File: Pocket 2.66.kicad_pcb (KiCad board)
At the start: 4 copper layers, 45 x 29.2 mm, 85 parts, among them P1 USB-TYPE-C-018, P3 FPC-05F-24PH20, P4 HX-1.25-2AWB, Q1 HL2300, Q2 HL2305, SW1 TS-24CA-S16, SW2 TS-24CA-S16, SW3 TS-24CA-S16, U1 ESP32-C3FH4, U2 LCK-TF-027H30008-WLG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

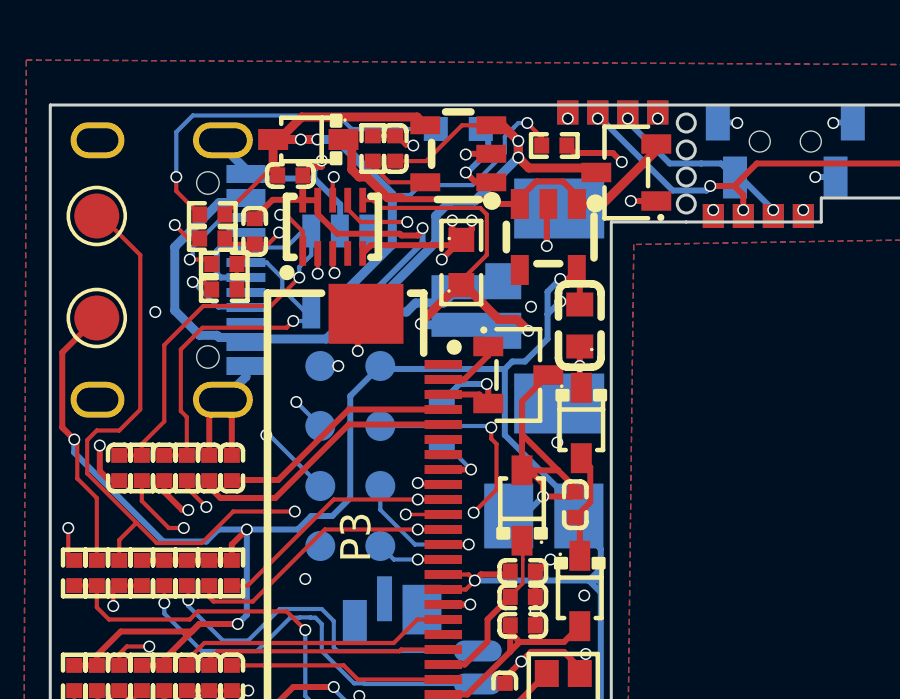
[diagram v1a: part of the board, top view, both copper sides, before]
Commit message: Move 2R2 basic part to top side
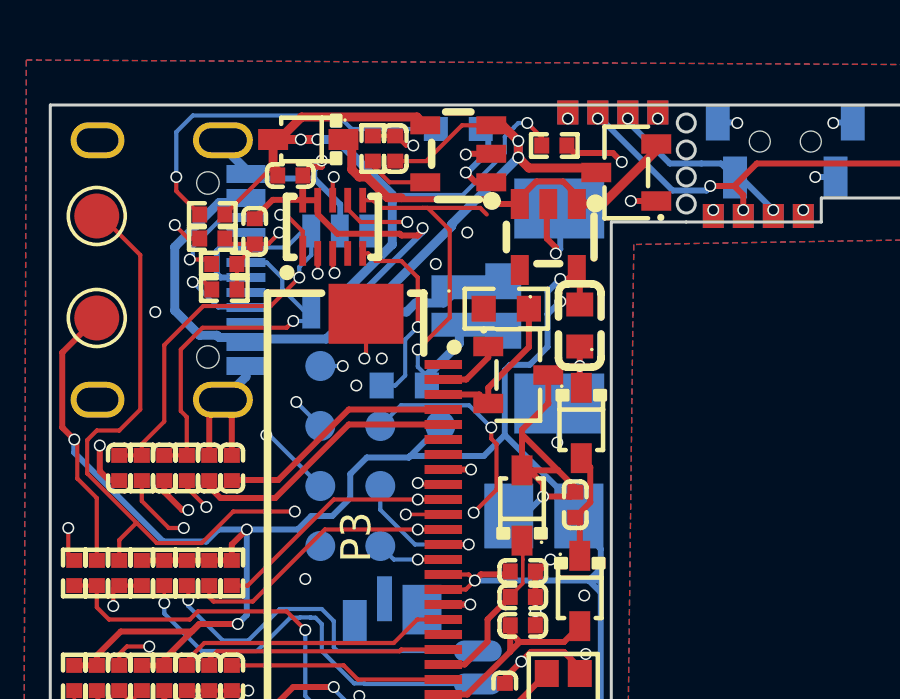
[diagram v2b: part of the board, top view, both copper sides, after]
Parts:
- R1: moved to F.Cu
- SH2: moved to B.Cu
- moved SH2 4.52 mm to (111.8, 80.2), turned to 0 degrees
- moved R1 4.42 mm to (115.2, 77.6), turned to 180 degrees
- moved TP9 2.83 mm to (113.0, 81.5)
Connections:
- TP1 pad 1: /DIS_DC -> /FLEX
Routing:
- net /RESE: track 4.04 -> 5.34 mm, vias 1 -> 0
- net /VBAT-: track 15.5 -> 14.7 mm, vias 2 -> 1
- net /BUT: track 53.8 -> 54.5 mm
- net 3V3: track 123.4 -> 122.8 mm
- net /BOOT: track 54.6 -> 55.2 mm
- net GND: track 85.3 -> 85.1 mm, vias 91 -> 92

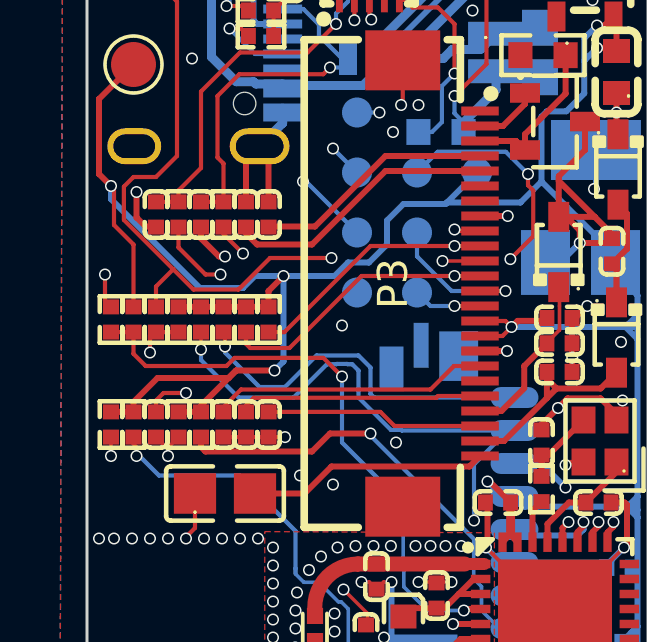
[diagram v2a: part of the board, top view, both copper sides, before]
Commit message: remove vias from serial no. area
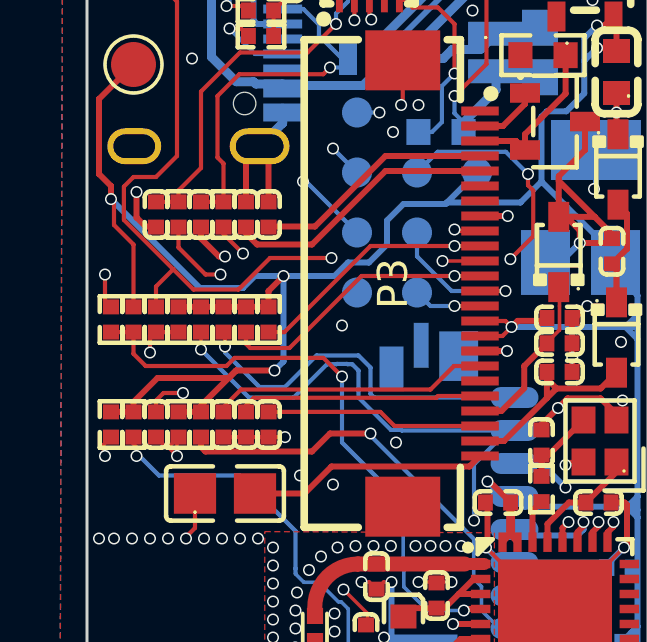
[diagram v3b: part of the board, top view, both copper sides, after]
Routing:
- net /EN: track 43.6 -> 44.1 mm

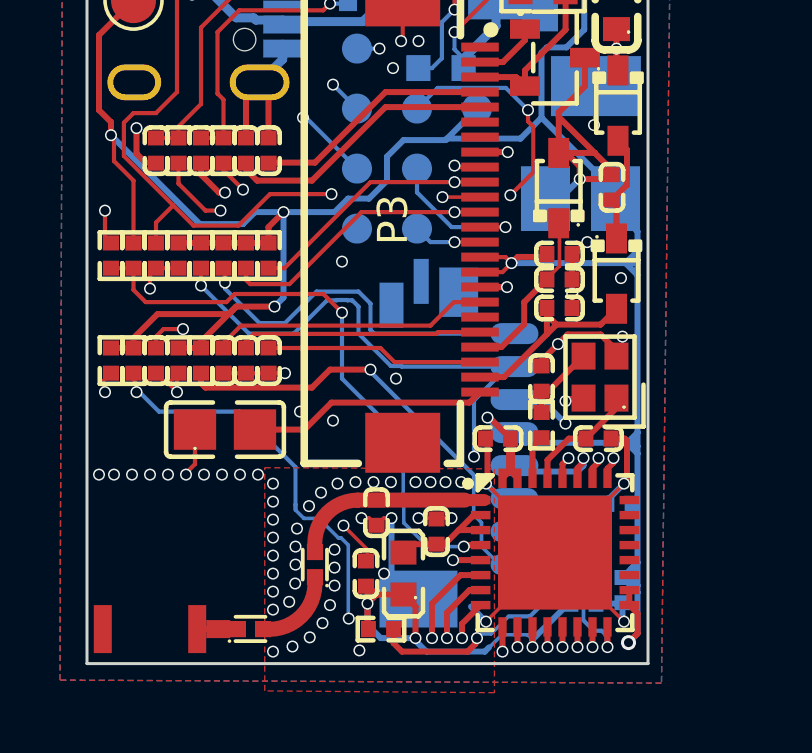
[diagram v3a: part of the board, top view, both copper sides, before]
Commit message: Add extra test pads
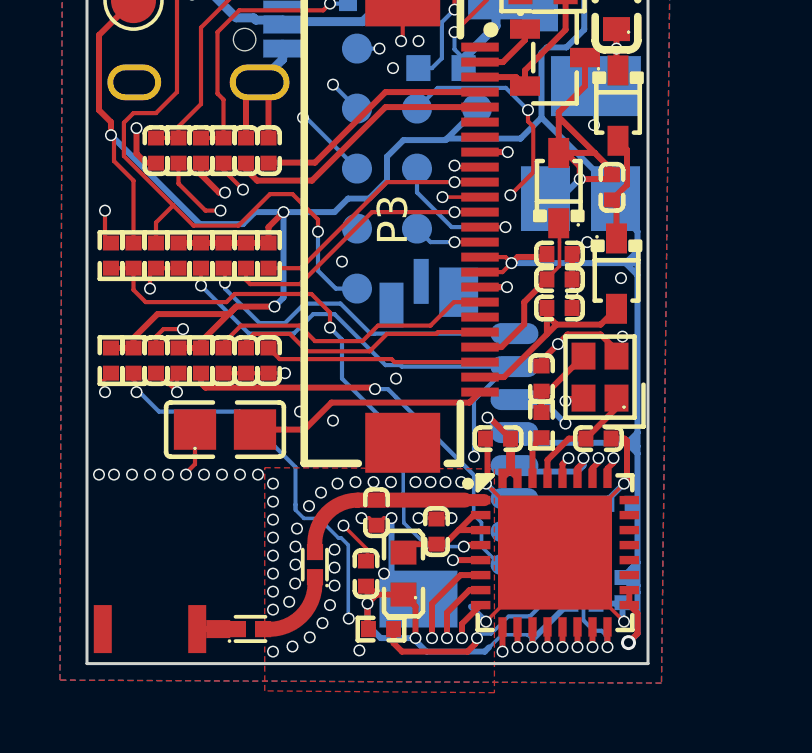
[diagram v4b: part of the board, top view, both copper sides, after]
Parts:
- added TP11: TestPoint, TestPoint:TestPoint_Pad_D1.0mm, B.Cu at (109.0, 87.5)
- added TP12: TestPoint, TestPoint:TestPoint_Pad_D1.0mm, B.Cu at (116.3, 96.9)
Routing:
- net /FLEX: track 38.9 -> 41.0 mm
- net /SD_CS: track 22.4 -> 21.5 mm
- net /DAT2: track 12.4 -> 11.5 mm
- net /DAT1: track 15.1 -> 14.5 mm

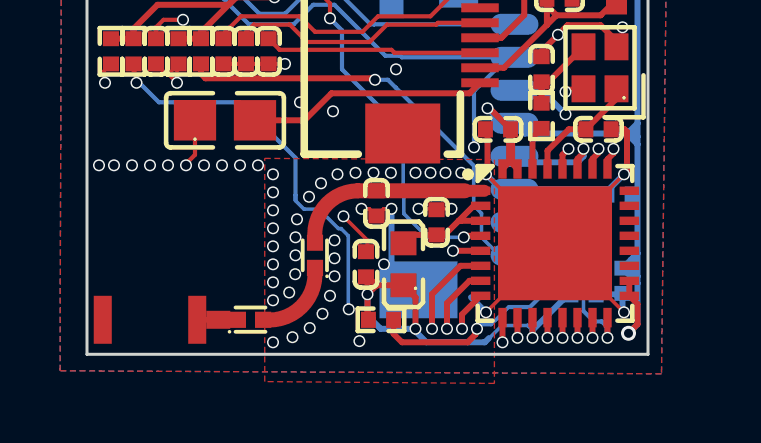
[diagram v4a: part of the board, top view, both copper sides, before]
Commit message: Add second RF shunt (DNP) for extra matching flexibility
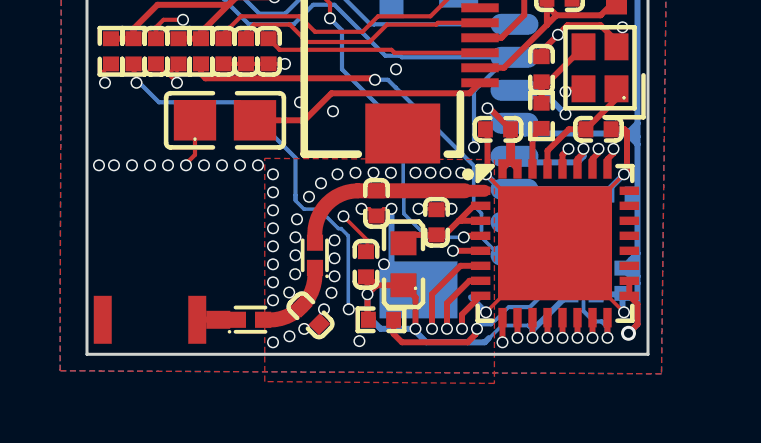
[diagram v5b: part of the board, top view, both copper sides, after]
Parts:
- added C23: 0.7pF 0402, LCSC:C0402, F.Cu at (107.5, 98.7)

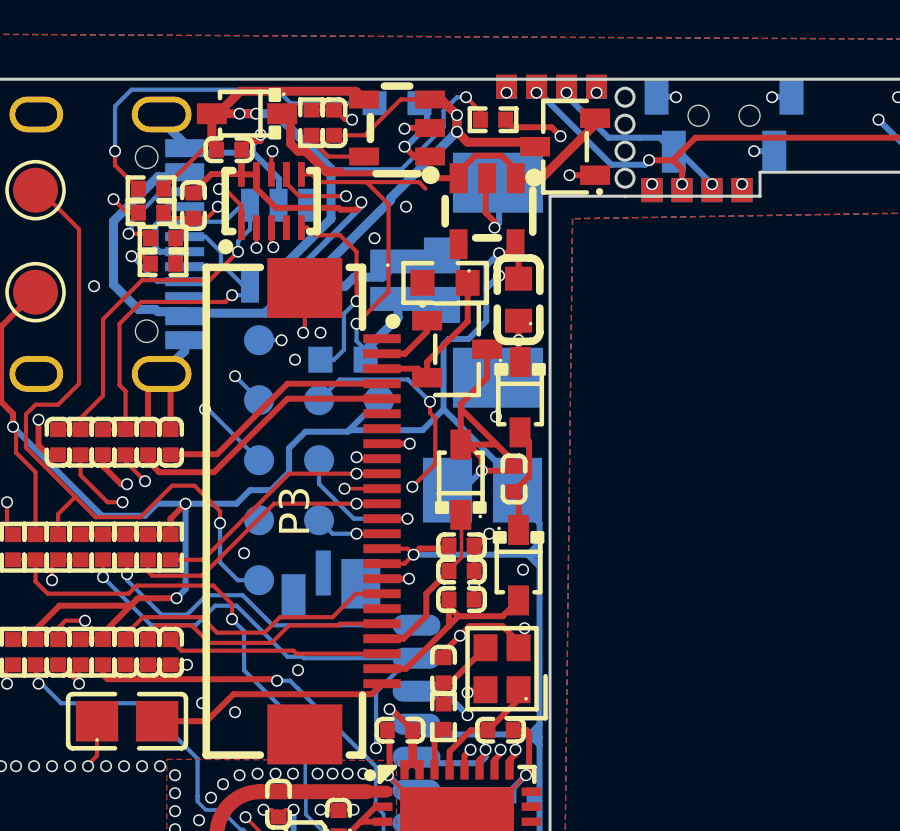
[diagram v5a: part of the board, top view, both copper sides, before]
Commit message: Remove floating traces
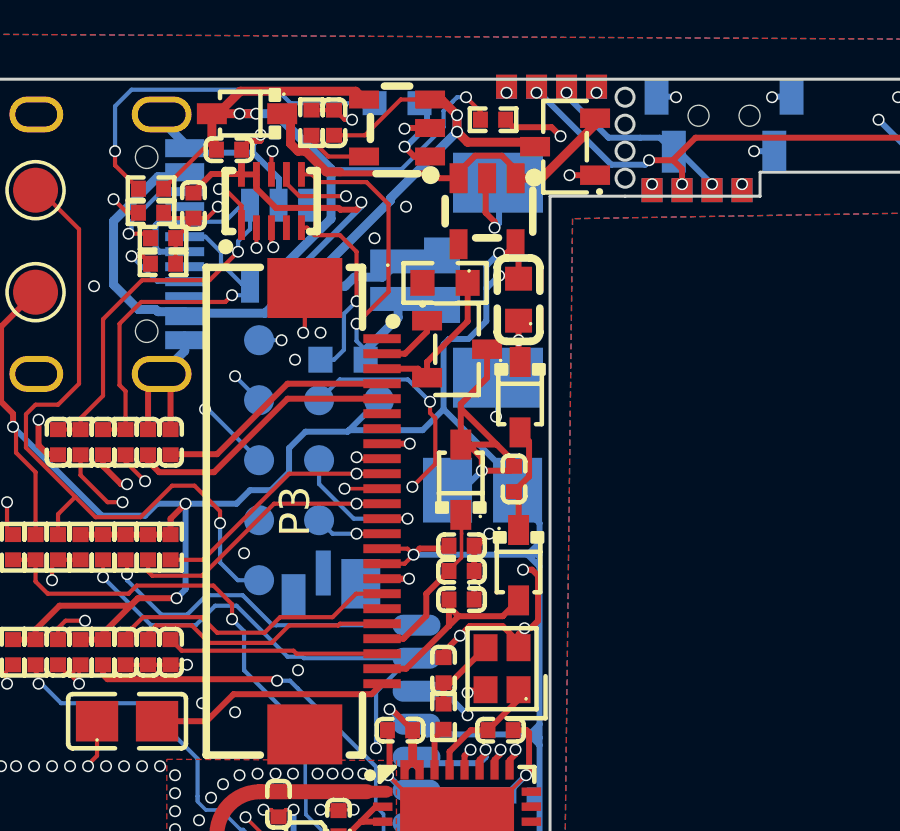
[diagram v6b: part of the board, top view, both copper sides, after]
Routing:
- net GND: track 85.0 -> 88.3 mm
- net /VBAT-: track 14.7 -> 12.4 mm
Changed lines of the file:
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@@
 	)
 	(segment
+		(start 118.05 89.1)
+		(end 118.3 88.85)
+		(width 0.2)
+		(layer "F.Cu")
+		(net "GND")
+	)
+	(segment
 		(start 113.1 87.450064)
 		(end 113.999936 87.450064)
@@
 	)
 	(segment
+		(start 118.3 88.85)
+		(end 118.3 87.35)
+		(width 0.2)
+		(layer "F.Cu")
+		(net "GND")
+	)
+	(segment
 		(start 106.05 82.479883)
 		(end 106.05 80.920873)
@@
 	)
 	(segment
+		(start 117.649911 89.749975)
+		(end 117.649911 89.300089)
+		(width 0.2)
+		(layer "F.Cu")
+		(net "GND")
+	)
+	(segment
 		(start 115.7 89.35)
 		(end 115.15 89.9)
@@
 	)
 	(segment
+		(start 117.649911 89.300089)
+		(end 117.85 89.1)
+		(width 0.2)
+		(layer "F.Cu")
+		(net "GND")
+	)
+	(segment
 		(start 115.6 96.3)
 		(end 117.75 98.45)
@@
 	)
 	(segment
+		(start 117.85 89.1)
+		(end 118.05 89.1)
+		(width 0.2)
+		(layer "F.Cu")
+		(net "GND")
+	)
+	(segment
 		(start 112.25 76.55)
 		(end 112.25 78.2)
@@
 	)
 	(segment
+		(start 118.1 87.15)
+		(end 117.8 87.15)
+		(width 0.2)
+		(layer "F.Cu")
+		(net "GND")
+	)
+	(segment
 		(start 116.275 86.35)
 		(end 116.675 85.95)
@@
 	)
 	(segment
+		(start 118.3 87.35)
+		(end 118.1 87.15)
+		(width 0.2)
+		(layer "F.Cu")
+		(net "GND")
+	)
+	(segment
 		(start 117.65 78.650025)
 		(end 117.65 80.177534)
@@
 	)
 	(segment
-		(start 114.55 74.45)
-		(end 114.33 74.23)
-		(width 0.14)
-		(layer "F.Cu")
-		(net "/VBAT-")
-	)
-	(segment
 		(start 112.58 74.23)
 		(end 112.4 74.23)
@@
 		(width 0.14)
 		(layer "F.Cu")
-		(net "/VBAT-")
-	)
-	(segment
-		(start 114.33 74.23)
-		(end 112.4 74.23)
-		(width 0.14)
-		(layer "F.Cu")

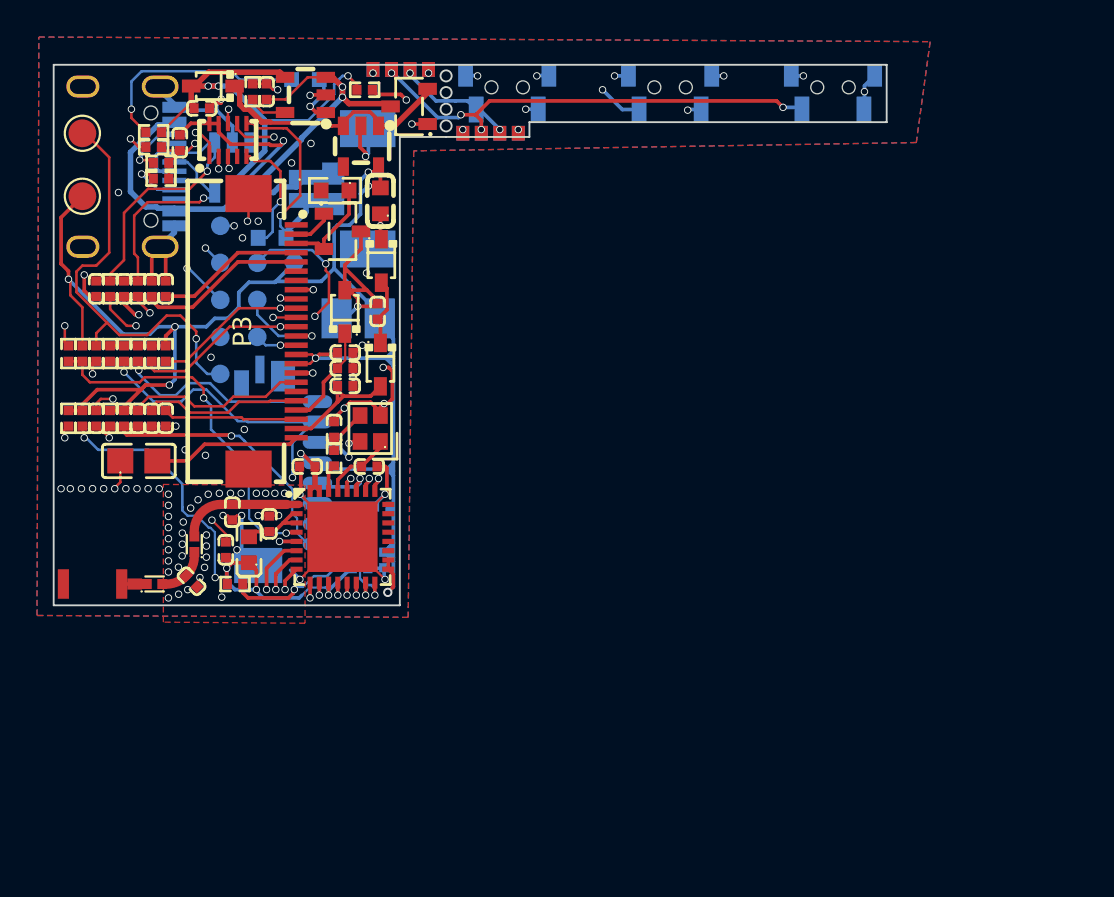
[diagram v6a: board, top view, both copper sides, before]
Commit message: Schematics for ESP32-C3 mini module
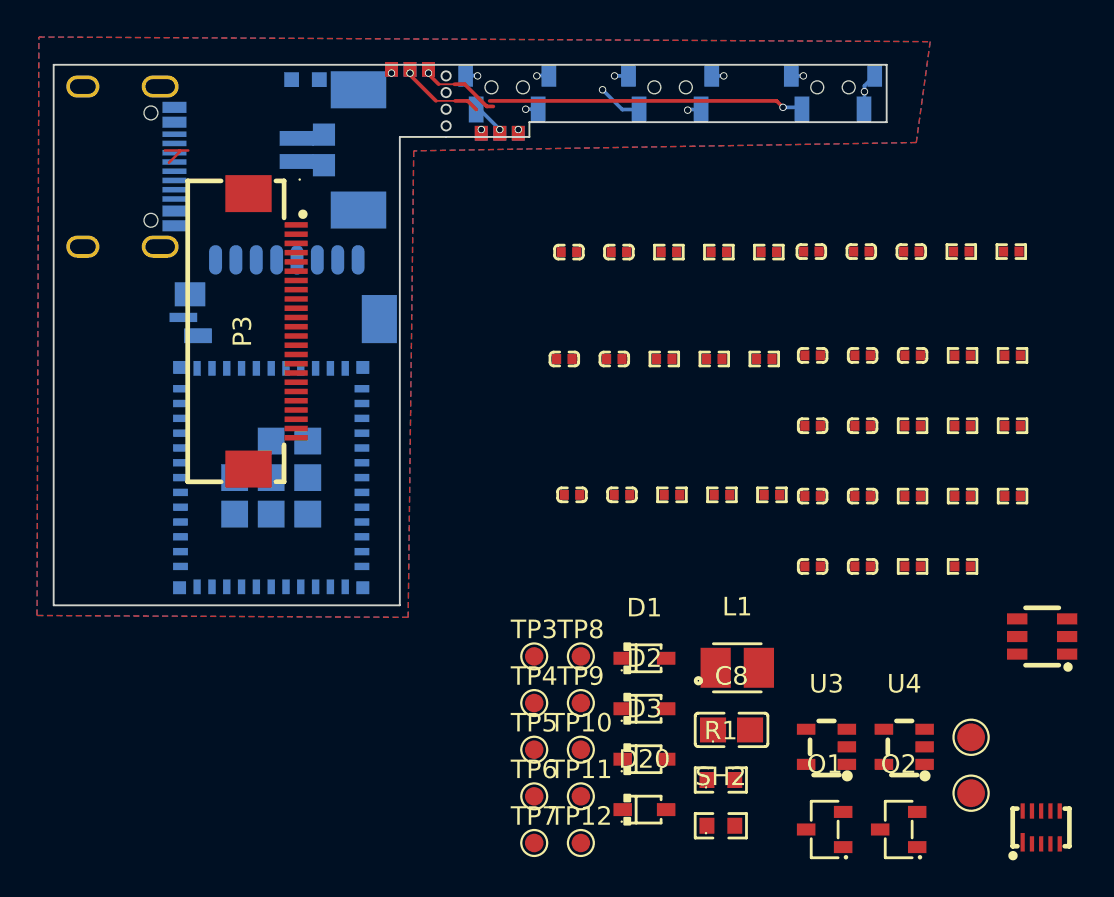
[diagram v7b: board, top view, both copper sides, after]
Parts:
- removed ANT2: 2.45 Ghz 1206, LCSC:SMD_ANT_1206
- removed C10: 0.7pF 0402, LCSC:C0402
- removed C14, C15, C18: 1uF, LCSC:C0402
- removed C16, C17: 15pF, LCSC:C0402
- removed C19, C24: 4.7uF 10V, LCSC:C0402
- removed FB1: BLM18PG121SN1D_C14709, LCSC:C14709_L0603
- removed L2: 8.2nH 0402, LCSC:L0402
- removed L3: 1.6nH 0402, LCSC:L0402
- removed R15, R16, R17: 10KΩ, LCSC:R0402
- removed X1: 40MHz 9pF 2016, LCSC:C49304717_CRYSTAL-SMD_4P-L2_0-W1_6-BL
- added R24: 10KΩ, LCSC:R0402, F.Cu at (151.8, 94.1)
- added R4: 10KΩ, LCSC:R0402, F.Cu at (133.0, 86.7)
- C11, C12: value 1uF -> 4.7uF 10V
- C13, L1, SH2, TP10, TP11, TP12, TP3, TP4, TP5, TP6, TP7, TP8, TP9, U6: moved to F.Cu
- C21: value 22uF -> 4.7uF 10V; footprint LCSC:C59461_C0603 -> LCSC:C0402
- C23: value 0.7pF 0402 -> 4.7uF 10V
- R18: value 22Ω -> 10KΩ
- U1: value ESP32-C3FH4 -> ESP32-C3-MINI-1-N4; footprint LCSC:C2858491_QFN-32_L5_0-W5_0-P0_50-TL-EP3_7 -> LCSC:C2838502_WIFIM-SMD_ESP32-C3-MINI-1; moved to B.Cu
- moved TP1 58.0 mm to (149.6, 107.1)
- moved TP2 57.8 mm to (149.6, 110.2)
- moved U5 57.5 mm to (153.3, 112.0)
- moved U6 50.6 mm to (153.4, 101.7), turned to 0 degrees
- moved R8 48.3 mm to (149.0, 80.9), turned to 0 degrees
- moved Q2 47.2 mm to (145.7, 112.1)
- moved R19 46.7 mm to (151.7, 80.9)
- moved R5 45.8 mm to (146.4, 94.1), turned to 0 degrees
- moved D20 45.5 mm to (131.9, 111.0), turned to 0 degrees
- moved R13 45.5 mm to (149.1, 94.1), turned to 0 degrees
- moved R11 45.5 mm to (149.1, 90.3), turned to 0 degrees
- moved U3 45.1 mm to (141.8, 107.6)
- moved R9 44.5 mm to (149.1, 86.5)
- moved R7 44.5 mm to (146.4, 97.9), turned to 0 degrees
- moved C30 44.1 mm to (146.3, 80.9), turned to 0 degrees
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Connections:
- C11 pad 2: /VDD3P3 -> 3V3
- C12 pad 2: 3V3 -> /EN
- C22 pad 2: /VBAT -> VUSB
- C23 pad 2: Net-(C23-Pad2) -> /VBAT
- R18 pad 1: /X1_PI -> /ALM
- R18 pad 2: /X1_P -> 3V3
- U1 pad 1: /LNA_IN -> GND
- U1 pad 10: /BUSY -> unconnected-(U1-NC-Pad10)
- U1 pad 11: 3V3 -> GND
- U1 pad 12: /DIS_RS -> /BUT
- U1 pad 13: /DIS_DC -> /SD_CS
- U1 pad 14: /DIS_CS -> GND
- U1 pad 15: /BOOT -> unconnected-(U1-NC-Pad15)
- U1 pad 17: 3V3 -> unconnected-(U1-NC-Pad17)
- U1 pad 18: 3V3 -> /FLEX
- U1 pad 19: unconnected-(U1-SPIHD-Pad19) -> /BUSY
- U1 pad 2: /VDD3P3 -> GND
- U1 pad 20: unconnected-(U1-SPIWP-Pad20) -> /DIS_RS
- U1 pad 21: unconnected-(U1-SPICS0-Pad21) -> /DIS_DC
- U1 pad 22: unconnected-(U1-SPICLK-Pad22) -> /DIS_CS
- U1 pad 23: unconnected-(U1-SPID-Pad23) -> /BOOT
- U1 pad 25: /U- -> unconnected-(U1-NC-Pad25)
- U1 pad 26: /U+ -> /U-
- U1 pad 27: /SCK -> /U+
- U1 pad 28: /MOSI -> unconnected-(U1-NC-Pad28)
- U1 pad 29: /X1_N -> unconnected-(U1-NC-Pad29)
- U1 pad 3: /VDD3P3 -> 3V3
- U1 pad 30: /X1_P -> /SCK
- U1 pad 31: 3V3 -> /MOSI
- U1 pad 32: 3V3 -> unconnected-(U1-NC-Pad32)
- U1 pad 33: GND -> unconnected-(U1-NC-Pad33)
- U1 pad 4: /BUT -> unconnected-(U1-NC-Pad4)
- U1 pad 5: /SD_CS -> /SDA
- U1 pad 6: /SDA -> /SCL
- U1 pad 7: /EN -> unconnected-(U1-NC-Pad7)
- U1 pad 8: /SCL -> /EN
- U1 pad 9: /FLEX -> unconnected-(U1-NC-Pad9)
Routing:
- net 3V3: track 122.4 -> 0.00 mm, vias 11 -> 0
- net GND: track 88.3 -> 9.16 mm, vias 92 -> 10
- net /BUT: track 54.6 -> 5.56 mm, vias 4 -> 2
- net /EN: track 44.1 -> 0.00 mm, vias 4 -> 0
- net /SCL: track 41.5 -> 0.00 mm, vias 5 -> 0
- net /BOOT: track 55.2 -> 14.0 mm, vias 6 -> 3
- net /FLEX: track 41.0 -> 0.00 mm, vias 2 -> 0
- net /SDA: track 40.9 -> 0.14 mm, vias 4 -> 0
- net VUSB: track 38.4 -> 0.00 mm, vias 3 -> 0
- net /BUT2: track 50.8 -> 17.1 mm, vias 5 -> 1
- net /VBAT: track 28.8 -> 0.00 mm, vias 3 -> 0
- net /DIS_RS: track 28.0 -> 0.00 mm, vias 2 -> 0
- net /DIS_CS: track 27.3 -> 0.00 mm, vias 2 -> 0
- net /U+: track 26.9 -> 0.00 mm, vias 2 -> 0
- net /U-: track 25.5 -> 0.00 mm, vias 2 -> 0
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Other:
- outline, holes or cut-outs redrawn
